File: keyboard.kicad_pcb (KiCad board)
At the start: 2 copper layers, 29 parts, among them SW1 SW_Push, SW10 SW_Push, SW11 SW_Push, SW12 SW_Push, SW13 SW_Push, SW14 SW_Push, SW15 SW_Push, SW16 SW_Push, SW17 SW_Push, SW18 SW_Push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

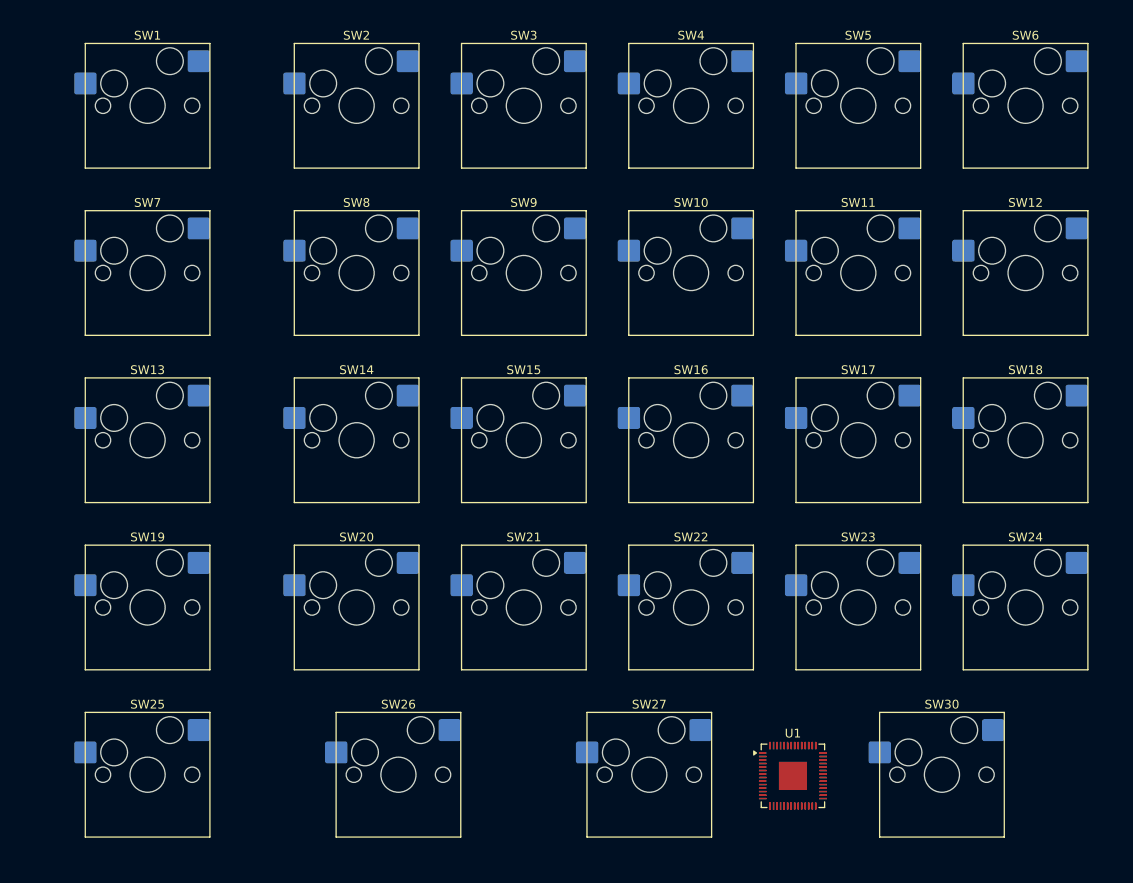
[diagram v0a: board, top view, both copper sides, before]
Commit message: Wired rows and columns and added i2c pinheader
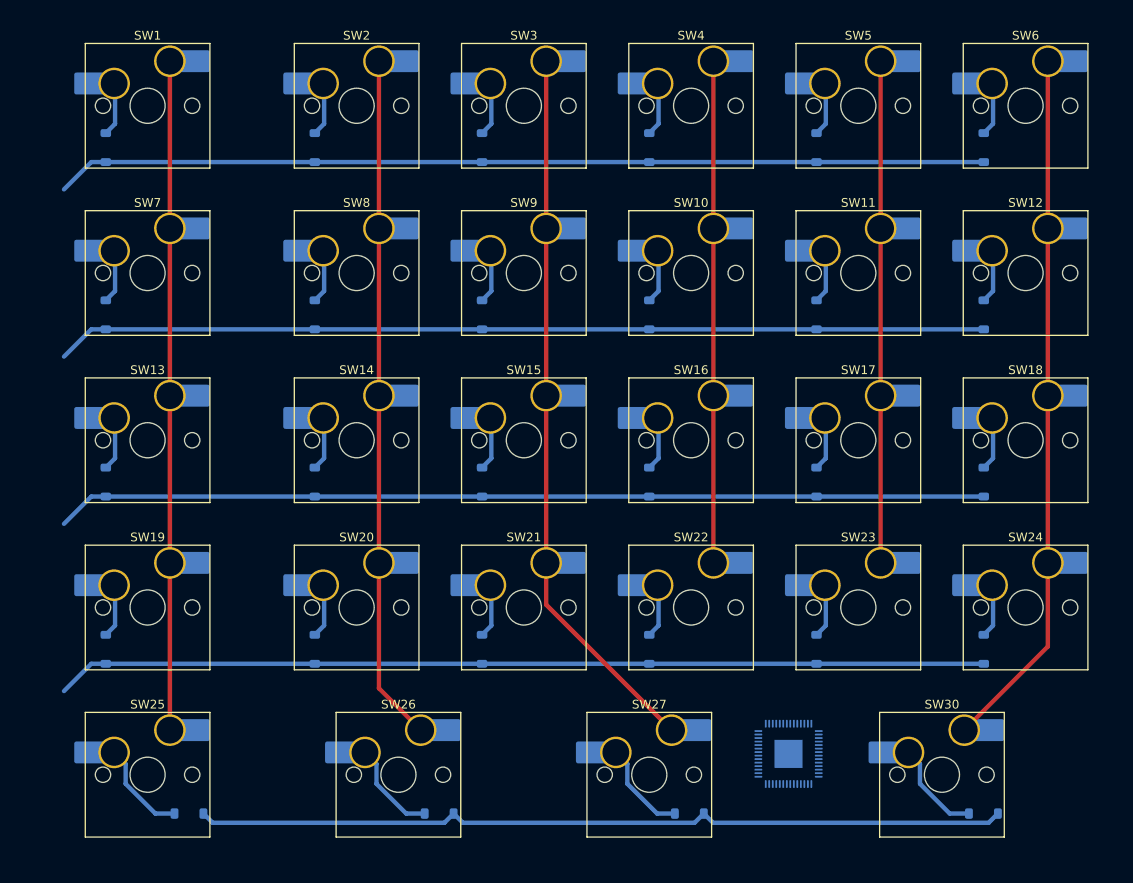
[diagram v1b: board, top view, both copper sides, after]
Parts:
- added D1: D, Diode_SMD:D_SOD-123, B.Cu at (24.1, 28.6)
- added D10: D, Diode_SMD:D_SOD-123, B.Cu at (86.0, 47.6)
- added D11: D, Diode_SMD:D_SOD-123, B.Cu at (105.1, 47.6)
- added D12: D, Diode_SMD:D_SOD-123, B.Cu at (124.1, 47.6)
- added D13: D, Diode_SMD:D_SOD-123, B.Cu at (24.1, 66.7)
- added D14: D, Diode_SMD:D_SOD-123, B.Cu at (47.9, 66.7)
- added D15: D, Diode_SMD:D_SOD-123, B.Cu at (67.0, 66.7)
- added D16: D, Diode_SMD:D_SOD-123, B.Cu at (86.0, 66.7)
- added D17: D, Diode_SMD:D_SOD-123, B.Cu at (105.1, 66.7)
- added D18: D, Diode_SMD:D_SOD-123, B.Cu at (124.1, 66.7)
- added D19: D, Diode_SMD:D_SOD-123, B.Cu at (24.1, 85.7)
- added D2: D, Diode_SMD:D_SOD-123, B.Cu at (47.9, 28.6)
- added D20: D, Diode_SMD:D_SOD-123, B.Cu at (47.9, 85.7)
- added D21: D, Diode_SMD:D_SOD-123, B.Cu at (67.0, 85.7)
- added D22: D, Diode_SMD:D_SOD-123, B.Cu at (86.0, 85.7)
- added D23: D, Diode_SMD:D_SOD-123, B.Cu at (105.1, 85.7)
- added D24: D, Diode_SMD:D_SOD-123, B.Cu at (124.1, 85.7)
- added D25: D, Diode_SMD:D_SOD-123, B.Cu at (33.6, 104.4)
- added D26: D, Diode_SMD:D_SOD-123, B.Cu at (62.1, 104.4)
- added D27: D, Diode_SMD:D_SOD-123, B.Cu at (90.6, 104.4)
- added D3: D, Diode_SMD:D_SOD-123, B.Cu at (67.0, 28.6)
- added D30: D, Diode_SMD:D_SOD-123, B.Cu at (124.1, 104.4)
- added D4: D, Diode_SMD:D_SOD-123, B.Cu at (86.0, 28.6)
- added D5: D, Diode_SMD:D_SOD-123, B.Cu at (105.1, 28.6)
- added D6: D, Diode_SMD:D_SOD-123, B.Cu at (124.1, 28.6)
- added D7: D, Diode_SMD:D_SOD-123, B.Cu at (24.1, 47.6)
- added D8: D, Diode_SMD:D_SOD-123, B.Cu at (47.9, 47.6)
- added D9: D, Diode_SMD:D_SOD-123, B.Cu at (67.0, 47.6)
- SW1, SW13, SW19, SW25, SW26, SW27, SW7: footprint PCM_Switch_Keyboard_Hotswap_Kailh:SW_Hotswap_Kailh_MX_1.50u -> PCM_Switch_Keyboard_Hotswap_Kailh:SW_Hotswap_Kailh_MX_Plated_1.50u
- SW10, SW11, SW12, SW14, SW15, SW16, SW17, SW18, SW2, SW20, SW21, SW22, SW23, SW24, SW3, SW4, SW5, SW6, SW8, SW9: footprint PCM_Switch_Keyboard_Hotswap_Kailh:SW_Hotswap_Kailh_MX_1.00u -> PCM_Switch_Keyboard_Hotswap_Kailh:SW_Hotswap_Kailh_MX_Plated_1.00u
- SW30: footprint PCM_Switch_Keyboard_Hotswap_Kailh:SW_Hotswap_Kailh_MX_2.00u -> PCM_Switch_Keyboard_Hotswap_Kailh:SW_Hotswap_Kailh_MX_Plated_2.00u
- U1: moved to B.Cu
- moved U1 2.55 mm to (101.9, 97.6), turned to 180 degrees
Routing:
- net C1: track 0.00 -> 855.2 mm
- net R5: track 0.00 -> 93.1 mm
- net Net-(D30-A): track 0.00 -> 11.1 mm
- net Net-(D25-A): track 0.00 -> 11.1 mm
- net Net-(D26-A): track 0.00 -> 11.0 mm
- net Net-(D27-A): track 0.00 -> 10.9 mm
- net Net-(D15-A): track 0.00 -> 6.13 mm
- net Net-(D13-A): track 0.00 -> 6.13 mm
- net Net-(D9-A): track 0.00 -> 6.13 mm
- net Net-(D7-A): track 0.00 -> 6.13 mm
- net Net-(D21-A): track 0.00 -> 6.13 mm
- net Net-(D19-A): track 0.00 -> 6.13 mm
- net Net-(D1-A): track 0.00 -> 6.13 mm
- net Net-(D3-A): track 0.00 -> 6.13 mm
- net Net-(D16-A): track 0.00 -> 6.13 mm
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
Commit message: More wiring for the RP2040
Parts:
- added J1: Conn_01x04_Pin, Connector_PinHeader_2.54mm:PinHeader_1x04_P2.54mm_Vertical, B.Cu at (137.6, 43.7)
- added U2: USBLC6-2SC6, Package_TO_SOT_SMD:SOT-23-6, F.Cu at (130.7, 93.0)
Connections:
- U1 pad 11: unconnected-(U1-GPIO8-Pad11) -> C1
- U1 pad 12: unconnected-(U1-GPIO9-Pad12) -> C1
- U1 pad 13: unconnected-(U1-GPIO10-Pad13) -> R5
- U1 pad 2: unconnected-(U1-GPIO0-Pad2) -> C1
- U1 pad 27: unconnected-(U1-GPIO16-Pad27) -> SDA
- U1 pad 28: unconnected-(U1-GPIO17-Pad28) -> SCL
- U1 pad 3: unconnected-(U1-GPIO1-Pad3) -> C1
- U1 pad 4: unconnected-(U1-GPIO2-Pad4) -> C1
- U1 pad 46: unconnected-(U1-USB_DM-Pad46) -> DM
- U1 pad 47: unconnected-(U1-USB_DP-Pad47) -> DP
- U1 pad 5: unconnected-(U1-GPIO3-Pad5) -> C1
- U1 pad 6: unconnected-(U1-GPIO4-Pad6) -> C1
- U1 pad 7: unconnected-(U1-GPIO5-Pad7) -> C1
- U1 pad 8: unconnected-(U1-GPIO6-Pad8) -> C1
- U1 pad 9: unconnected-(U1-GPIO7-Pad9) -> C1
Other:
- board outline added: 125 x 96.5 mm
